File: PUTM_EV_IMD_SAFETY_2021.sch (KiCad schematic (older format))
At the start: 49 parts, among them J1 Conn_01x06, J2 Conn_01x02, K1 FINDER-30.22.7.005.0010, Q1 2N7002, U1 SN74LS32D, U10 74LVC1G79, U11 74LVC1G79, U2 MC78M12CDTG, U3 LM1117IMP-5.0, U4 LM393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

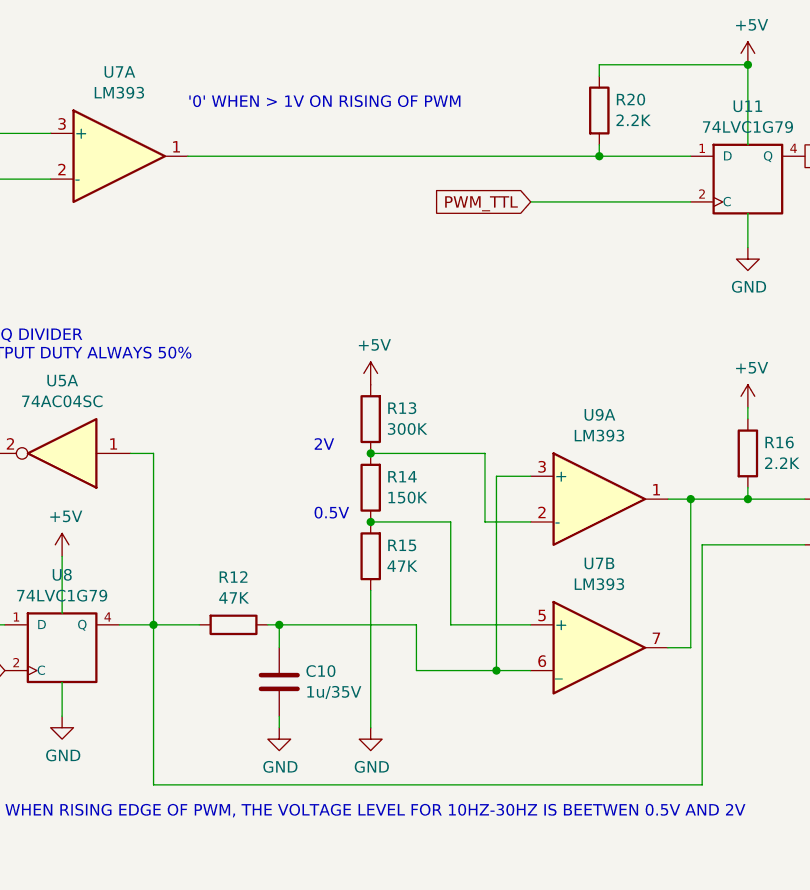
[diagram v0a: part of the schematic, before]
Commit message: schematic edited - changed comparator ladder connections
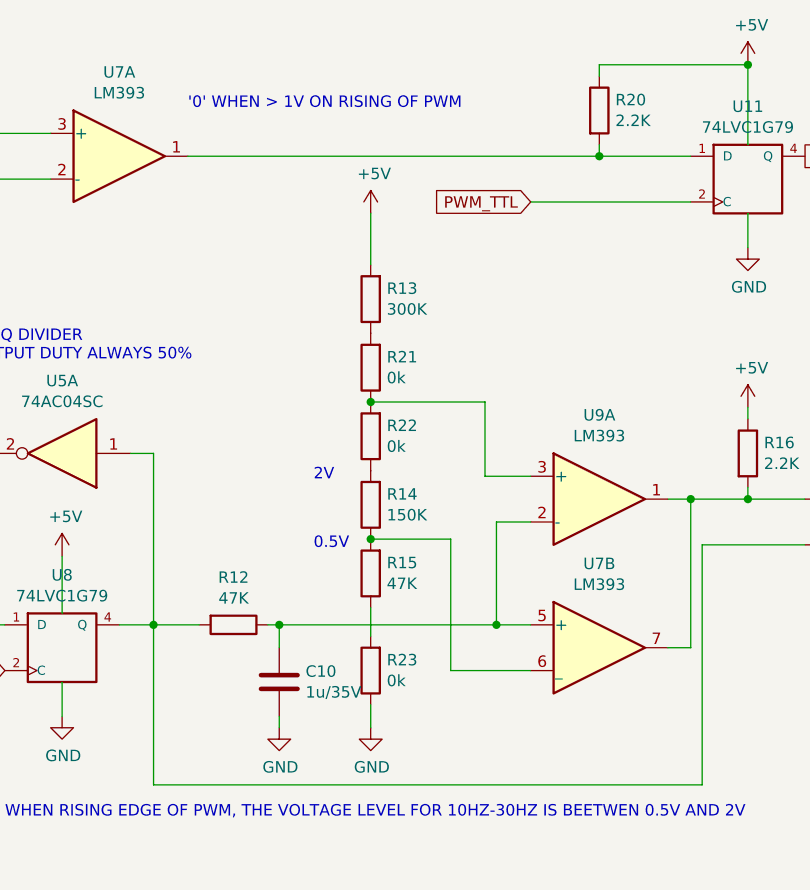
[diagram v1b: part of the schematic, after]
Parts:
- added R21, R22, R23: 0k, Resistor_SMD:R_1206_3216Metric, symbol PUTM_EV_IMD_SAFETY_2021-rescue:R-Device
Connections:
- net GND: now also R23.1; no longer R15.1
- net at C10.1, R12.1: now also U7.5 (+), U9.2 (-); no longer U7.6 (_), U9.3 (+)
- net at R14.1, R15.2: now also U7.6 (_); no longer U7.5 (+)
- new net: R21.1, R22.2, U9.3 (+)
- new net: R14.2, R22.1
- new net: R15.1, R23.2
- new net: R13.1, R21.2
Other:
- moved on the sheet: R13, R14, R15
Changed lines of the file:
@@
 EESchema Schematic File Version 4
-LIBS:PUTM_EV_IMD_SAFETY_2021-cache
 EELAYER 30 0
 EELAYER END
@@
 L PUTM_EV_IMD_SAFETY_2021-rescue:R-Device R14
 U 1 1 61677A2B
-P 7800 4900
-F 0 "R14" H 7730 4854 50  0000 R CNN
-F 1 "150K" H 7730 4945 50  0000 R CNN
-F 2 "Resistor_SMD:R_1206_3216Metric" V 7730 4900 50  0001 C CNN
-F 3 "~" H 7800 4900 50  0001 C CNN
-	1    7800 4900
+P 7800 4975
+F 0 "R14" H 7730 4929 50  0000 R CNN
+F 1 "150K" H 7730 5020 50  0000 R CNN
+F 2 "Resistor_SMD:R_1206_3216Metric" V 7730 4975 50  0001 C CNN
+F 3 "~" H 7800 4975 50  0001 C CNN
+	1    7800 4975
 	-1   0    0    1
 $EndComp
@@
 L PUTM_EV_IMD_SAFETY_2021-rescue:R-Device R15
 U 1 1 61677E14
-P 7800 5200
-F 0 "R15" H 7730 5154 50  0000 R CNN
-F 1 "47K" H 7730 5245 50  0000 R CNN
-F 2 "Resistor_SMD:R_1206_3216Metric" V 7730 5200 50  0001 C CNN
-F 3 "~" H 7800 5200 50  0001 C CNN
-	1    7800 5200
+P 7800 5275
+F 0 "R15" H 7730 5229 50  0000 R CNN
+F 1 "47K" H 7730 5320 50  0000 R CNN
+F 2 "Resistor_SMD:R_1206_3216Metric" V 7730 5275 50  0001 C CNN
+F 3 "~" H 7800 5275 50  0001 C CNN
+	1    7800 5275
 	-1   0    0    1
 $EndComp
@@
 L PUTM_EV_IMD_SAFETY_2021-rescue:R-Device R13
 U 1 1 6167819B
-P 7800 4600
-F 0 "R13" H 7730 4554 50  0000 R CNN
-F 1 "300K" H 7730 4645 50  0000 R CNN
-F 2 "Resistor_SMD:R_1206_3216Metric" V 7730 4600 50  0001 C CNN
-F 3 "~" H 7800 4600 50  0001 C CNN
-	1    7800 4600
+P 7800 4075
+F 0 "R13" H 7730 4029 50  0000 R CNN
+F 1 "300K" H 7730 4120 50  0000 R CNN
+F 2 "Resistor_SMD:R_1206_3216Metric" V 7730 4075 50  0001 C CNN
+F 3 "~" H 7800 4075 50  0001 C CNN
+	1    7800 4075
 	-1   0    0    1
 $EndComp
@@
 	1    0    0    -1
 $EndComp
-Wire Wire Line
-	7800 5350 7800 5950
 $Comp
 L PUTM_EV_IMD_SAFETY_2021-rescue:+5V-power #PWR030
 U 1 1 6167EB0A
-P 7800 4450
-F 0 "#PWR030" H 7800 4300 50  0001 C CNN
-F 1 "+5V" H 7815 4623 50  0000 C CNN
-F 2 "" H 7800 4450 50  0001 C CNN
-F 3 "" H 7800 4450 50  0001 C CNN
-	1    7800 4450
-	1    0    0    -1
-$EndComp
-Wire Wire Line
-	7800 4750 8300 4750
-Wire Wire Line
-	8300 5050 8500 5050
-Connection ~ 7800 4750
-Wire Wire Line
-	7800 5050 8150 5050
-Wire Wire Line
-	8150 5050 8150 5500
-Wire Wire Line
-	8150 5500 8500 5500
-Connection ~ 7800 5050
-Text Notes 7550 4750 0    50   ~ 0
+P 7800 3700
+F 0 "#PWR030" H 7800 3550 50  0001 C CNN
+F 1 "+5V" H 7815 3873 50  0000 C CNN
+F 2 "" H 7800 3700 50  0001 C CNN
+F 3 "" H 7800 3700 50  0001 C CNN
+	1    7800 3700
+	1    0    0    -1
+$EndComp
+Wire Wire Line
+	7800 4525 8300 4525
+Wire Wire Line
+	8300 4850 8500 4850
+Wire Wire Line
+	7800 5125 8150 5125
+Text Notes 7550 4875 0    50   ~ 0
 2V
-Text Notes 7550 5050 0    50   ~ 0
+Text Notes 7550 5175 0    50   ~ 0
 0.5V
 Text Notes 6200 6350 0    50   ~ 0
@@
 	6850 6200 9250 6200
 Wire Wire Line
-	8300 4750 8300 5050
-Wire Wire Line
-	8500 4850 8350 4850
-Wire Wire Line
-	8350 4850 8350 5700
-Wire Wire Line
-	8350 5700 8500 5700
-Wire Wire Line
-	8350 5700 8000 5700
-Wire Wire Line
-	8000 5700 8000 5500
-Wire Wire Line
-	8000 5500 7400 5500
-Connection ~ 8350 5700
+	8500 5050 8350 5050
+Wire Wire Line
+	8350 5050 8350 5500
+Wire Wire Line
+	8350 5500 8500 5500
+Connection ~ 8350 5500
 Connection ~ 7400 5500
 Wire Wire Line
@@
 Wire Wire Line
 	3150 2350 3700 2350
+Wire Wire Line
+	7400 5500 8350 5500
+Wire Wire Line
+	8150 5700 8500 5700
+$Comp
+L PUTM_EV_IMD_SAFETY_2021-rescue:R-Device R21
+U 1 1 62A6D899
+P 7800 4375
+F 0 "R21" H 7730 4329 50  0000 R CNN
+F 1 "0k" H 7730 4420 50  0000 R CNN
+F 2 "Resistor_SMD:R_1206_3216Metric" V 7730 4375 50  0001 C CNN
+F 3 "~" H 7800 4375 50  0001 C CNN
+	1    7800 4375
+	-1   0    0    1
+$EndComp
+$Comp
+L PUTM_EV_IMD_SAFETY_2021-rescue:R-Device R22
+U 1 1 62AA6277
+P 7800 4675
+F 0 "R22" H 7730 4629 50  0000 R CNN
+F 1 "0k" H 7730 4720 50  0000 R CNN
+F 2 "Resistor_SMD:R_1206_3216Metric" V 7730 4675 50  0001 C CNN
+F 3 "~" H 7800 4675 50  0001 C CNN
+	1    7800 4675
+	-1   0    0    1
+$EndComp
+Connection ~ 7800 5125
+Connection ~ 7800 4525
+Wire Wire Line
+	8150 5125 8150 5700
+$Comp
+L PUTM_EV_IMD_SAFETY_2021-rescue:R-Device R23
+U 1 1 62AF5F32
+P 7800 5700
+F 0 "R23" H 7730 5654 50  0000 R CNN
+F 1 "0k" H 7730 5745 50  0000 R CNN
+F 2 "Resistor_SMD:R_1206_3216Metric" V 7730 5700 50  0001 C CNN
+F 3 "~" H 7800 5700 50  0001 C CNN
+	1    7800 5700
+	-1   0    0    1
+$EndComp
+Wire Wire Line
+	7800 5550 7800 5425
+Wire Wire Line
+	7800 5850 7800 5950
+Wire Wire Line
+	8300 4525 8300 4850
+Wire Wire Line
+	7800 3700 7800 3925
 $EndSCHEMATC

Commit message: Project converted to Kicad6, Schematic beatuyfing
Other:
- note added: "100k 1M i 100uF"
- note added: "Active Low"
- note added: "R"
- note added: "S"
- note added: "Tutaj dodać RC zeby zaburzenie\n wejscia nie zmienialo od razu wyjscia"
- note added: "Wiekszy pullup i kondensator powinny \nrozwiazac sprawe aby reset nastepowal\n od razu po zalaczeniu zasilania"
